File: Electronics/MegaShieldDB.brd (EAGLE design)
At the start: 100.3 x 80 mm, 40 parts, among them IC2 MCP4802, IC3 MCP4802, IC4 4013N, Q1 BF199, Q5 BF199, X1 M25-HD-20, X2 Brake, X4 Cruise Computers, X5 Steer, X6 Motor Controller

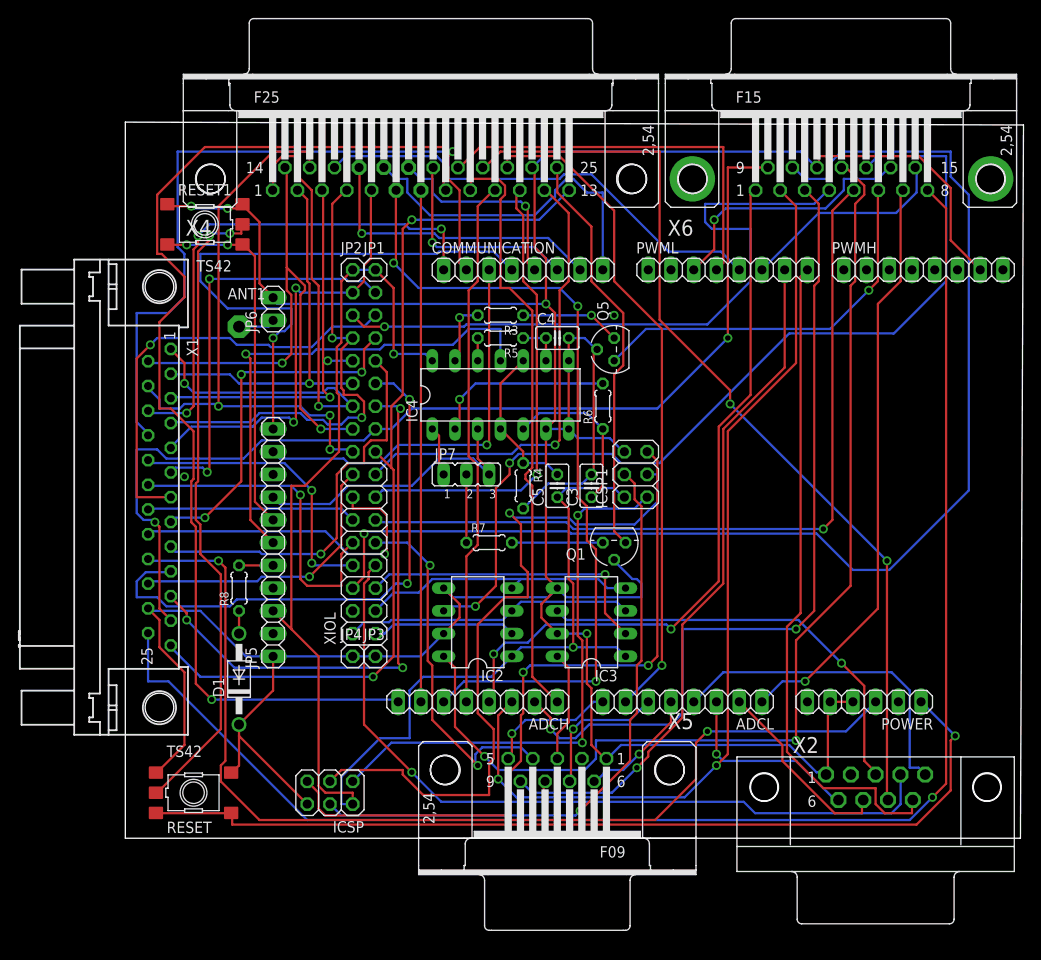
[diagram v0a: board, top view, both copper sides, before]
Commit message: Included holes for mounting Mega, board cutouts, renamed connectors. Signals to front panel have been swapped.  Connector names have changed.
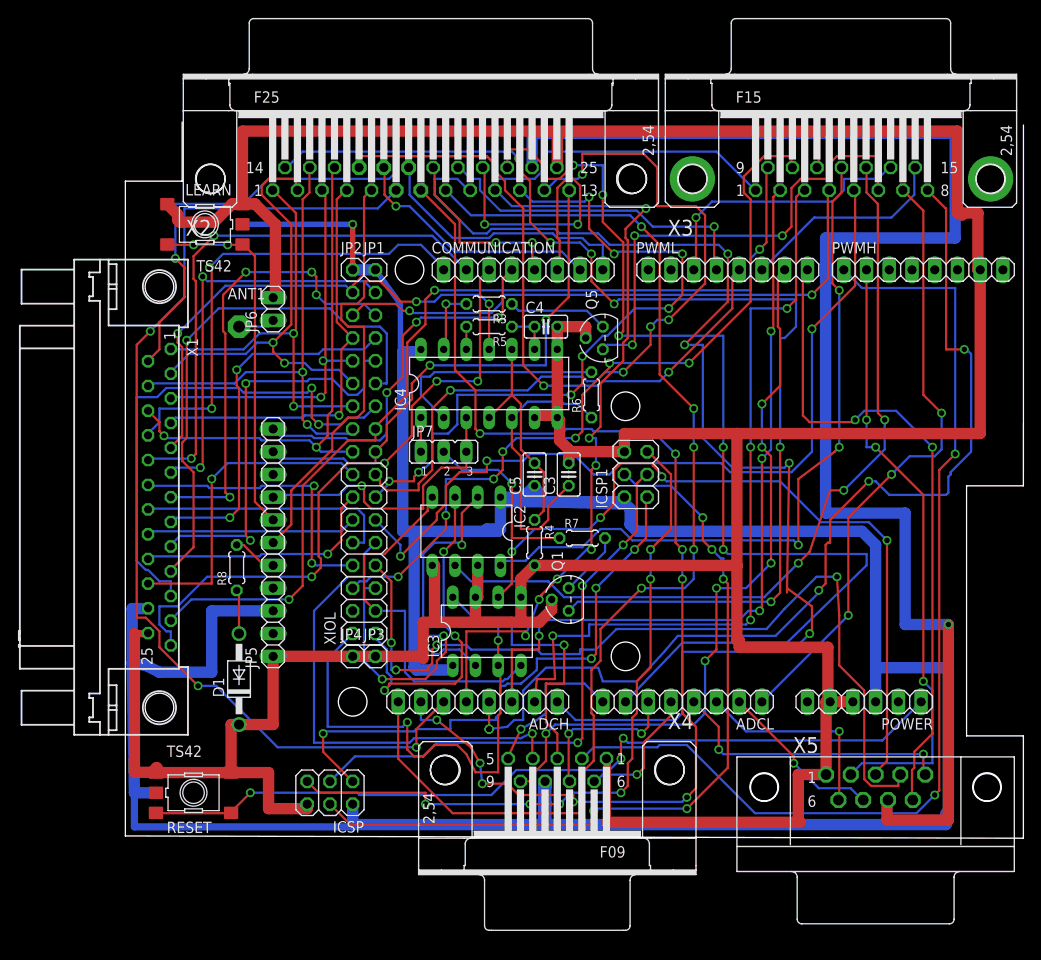
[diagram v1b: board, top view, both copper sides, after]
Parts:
- X2: value Brake -> Cruise Computers; device con-subd:182-009-MALE -> con-subd:F25H
- X4: value Cruise Computers -> Steer; device con-subd:F25H -> con-subd:F09H
- X5: value Steer -> Brake; device con-subd:F09H -> con-subd:182-009-MALE
- moved X2 92.6 mm to (33.0, 73.7)
- moved X4 67.8 mm to (48.3, 7.62), turned to 180 degrees
- moved X5 37.4 mm to (83.8, -3.81), turned to 0 degrees
- moved IC3 11.7 mm to (40.4, 23.1), turned to 0 degrees
- moved R7 10.4 mm to (51.1, 33.5)
- moved IC2 10.2 mm to (38.1, 34.3), turned to 180 degrees
- moved Q1 8.13 mm to (49.5, 26.7), turned to 90 degrees
- moved R4 6.48 mm to (45.7, 33.0)
- moved JP7 3.59 mm to (35.6, 43.2)
- moved C3 2.84 mm to (49.5, 40.6)
- moved C5 2.84 mm to (45.7, 40.6)
- moved R8 2.30 mm to (12.4, 30.2)
- moved R6 1.80 mm to (52.1, 49.5)
- moved Q5 1.80 mm to (53.3, 55.9)
- moved C4 1.80 mm to (47.0, 57.1)
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- renumbered RESET1 to LEARN, X6 to X3
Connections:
- removed net 5-GND: LEARN.5, RESET.5
- removed net VCC: POWER.3, X1.22, X5.8
- new net N$16: PWMH.2, X5.2
- new net N$17: PWMH.1, X4.2
- net +5V: now also LEARN.5, POWER.3, RESET.5, X1.24, X4.8
- net 5VBRK: now also X2.24, X5.8; no longer X2.8, X4.22
- net A1: now also X5.7; no longer X2.7
- net A11: now also X3.8; no longer X3.1
- net A12: now also X2.10; no longer X4.10
- net A13: now also X2.6; no longer X4.6
- net A14: now also X2.7; no longer X4.7
- net A15: now also X2.8; no longer X4.8
- net A4: now also X4.6; no longer X5.6
- net A5: now also X4.7; no longer X5.7
- net A6: now also X2.23; no longer X4.23
- net A7: now also X4.5; no longer X5.5
- net D14TXD3: now also X2.19; no longer X4.18
- net D15RXD3: now also X2.18; no longer X4.17
- net D16TXD2: now also X2.22; no longer X4.20
- net D17RXD2: now also X2.20; no longer X4.19
- net D20INT4: now also X1.18; no longer X1.17
- net D21INT5: now also X1.17; no longer X1.16
- net D23: now also X2.5; no longer X4.5
- net D27: now also X2.4; no longer X4.4
- net D29: now also X2.3; no longer X4.3
- net D31: now also X2.2; no longer X4.2
- net D33: now also X2.1; no longer X4.1
- net D35: now also X1.15, X2.15; no longer X1.14, X4.14
- net D36: now also X2.13; no longer X4.13
- net D37: now also X1.16, X2.16; no longer X1.15, X4.15
- net D39: now also X2.12; no longer X4.12
- net D3INT1: now also X2.21; no longer X4.21
- net D4: now also X2.17; no longer X4.16
- net D40: now also X1.22; no longer X1.21
- net D41: now also X2.11; no longer X4.11
- net D42: now also X1.21; no longer X1.20
- net D44: now also X1.20; no longer X1.19
- net D45: now also X4.4; no longer X5.4
- net D46: now also X1.19; no longer X1.18
- net D47: now also X5.4; no longer X2.4
- net D6: now also X4.9; no longer X5.9
- net D7: now also X5.9; no longer X2.9
- net DACC: now also X4.3; no longer X5.3
- net DACD: now also X5.3; no longer X2.3
- net FUEL: now also X1.14, X3.1; no longer X1.25, X3.8
- net GND: now also X1.25, X2.25, X4.1; no longer X1.24, X2.1, X4.24
- net N$1: now also X5.6; no longer X2.6
- net N$5: now also X2.9; no longer X4.9
- net N$8: now also X5.5; no longer X2.5
- net WLX: now also X2.14; no longer X4.25
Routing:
- net +5V: track 160.0 -> 352.0 mm, vias 2 -> 1
- net VCC: track 120.5 -> 0.00 mm, vias 2 -> 0
- net N$17: track 0.00 -> 114.9 mm, vias 0 -> 2
- net WLX: track 46.0 -> 128.6 mm, vias 0 -> 6
- net FUEL: track 169.8 -> 93.6 mm
- net A14: track 57.1 -> 130.2 mm, vias 0 -> 9
- net 5-GND: track 71.9 -> 0.00 mm, vias 2 -> 0
- net N$5: track 67.2 -> 136.2 mm, vias 0 -> 4
- net GND: track 390.8 -> 459.5 mm, vias 4 -> 0
- net N$16: track 0.00 -> 68.4 mm, vias 0 -> 3
- net 5VBRK: track 103.5 -> 165.2 mm, vias 2 -> 1
- net D48: track 138.8 -> 86.8 mm, vias 1 -> 7
- net A6: track 74.5 -> 122.1 mm, vias 1 -> 5
- net D52: track 32.4 -> 73.7 mm, vias 0 -> 3
- net DACA: track 119.6 -> 80.8 mm, vias 2 -> 3
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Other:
- outline, holes or cut-outs redrawn

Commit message: Mirrored Arduino pins for bottom mount. Added Wheel Revolution with pull-up resistor.
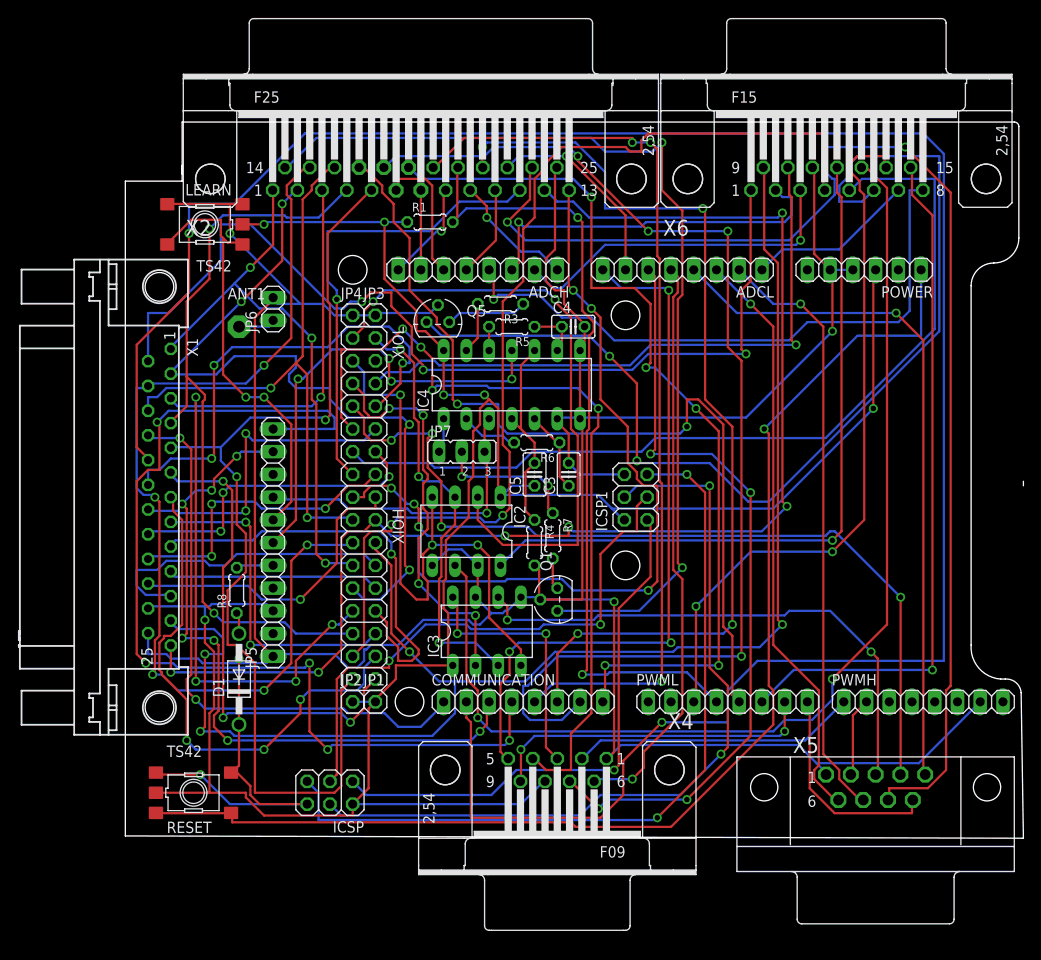
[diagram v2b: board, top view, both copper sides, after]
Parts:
- removed X3: Motor Controller, con-subd:F15HP
- added R1: 1M, rcl:0204/5
- added X6: (no value), con-subd:F15H
- moved ADCH 48.3 mm to (39.4, 63.5)
- moved ADCL 48.3 mm to (62.2, 63.5)
- moved COMMUNICATION 48.3 mm to (44.5, 15.2)
- moved JP1 48.3 mm to (27.9, 15.2)
- moved JP2 48.3 mm to (25.4, 15.2)
- moved POWER 48.3 mm to (82.5, 63.5)
- moved PWMH 48.3 mm to (89.2, 15.2)
- moved PWML 48.3 mm to (67.3, 15.2)
- moved JP3 38.1 mm to (27.9, 58.4)
- moved JP4 38.1 mm to (25.4, 58.4)
- moved XIOH 25.4 mm to (26.7, 26.7), flipped to the top, turned to 270 degrees
- moved Q5 18.5 mm to (34.9, 57.7), turned to 0 degrees
- moved XIOL 15.2 mm to (26.7, 47.0), turned to 270 degrees
- moved R6 8.10 mm to (46.0, 44.2), turned to 180 degrees
- moved R7 3.31 mm to (47.8, 33.8), turned to 270 degrees
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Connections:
- net N$16 renamed D9
- net N$17 renamed D8
- net +5V: now also R1.1
- net A0: now also X6.7; no longer X3.7
- net A10: now also X6.2; no longer X3.2
- net A11: now also X6.8; no longer X3.8
- net A9: now also X6.3; no longer X3.3
- net D25: now also X6.4; no longer X3.4
- net D2INT0: now also X6.14; no longer X3.14
- net D34: now also X6.9; no longer X3.9
- net D3INT1: now also R1.2
- net D43: now also X6.5; no longer X3.5
- net D48: now also X6.10; no longer X3.10
- net D5: now also X6.15; no longer X3.15
- net DACA: now also X6.12; no longer X3.12
- net DACB: now also X6.13; no longer X3.13
- net FUEL: now also X6.1; no longer X3.1
- net GND: now also X6.11; no longer X3.11
- net WLES: now also X6.6; no longer X3.6
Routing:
- net D20INT4: track 60.9 -> 254.3 mm
- net N$5: track 136.2 -> 14.2 mm, vias 4 -> 1
- net A14: track 130.2 -> 8.89 mm, vias 9 -> 0
- net A15: track 129.1 -> 11.5 mm, vias 5 -> 1
- net A13: track 117.0 -> 15.5 mm, vias 3 -> 0
- net D15RXD3: track 28.4 -> 128.0 mm, vias 1 -> 4
- net A6: track 122.1 -> 22.6 mm, vias 5 -> 1
- net +5V: track 352.0 -> 268.0 mm, vias 1 -> 6
- net D8: track 114.9 -> 31.9 mm, vias 2 -> 0
- net D17RXD2: track 21.0 -> 102.1 mm, vias 2 -> 3
- net A12: track 87.3 -> 10.4 mm, vias 7 -> 0
- net D16TXD2: track 34.0 -> 106.7 mm, vias 2 -> 4
- net D14TXD3: track 30.3 -> 100.7 mm, vias 0 -> 5
- net D18INT2: track 42.7 -> 112.4 mm, vias 3 -> 5
- net A5: track 17.9 -> 86.1 mm, vias 2 -> 4
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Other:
- outline, holes or cut-outs redrawn

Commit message: Rearranged jumper.
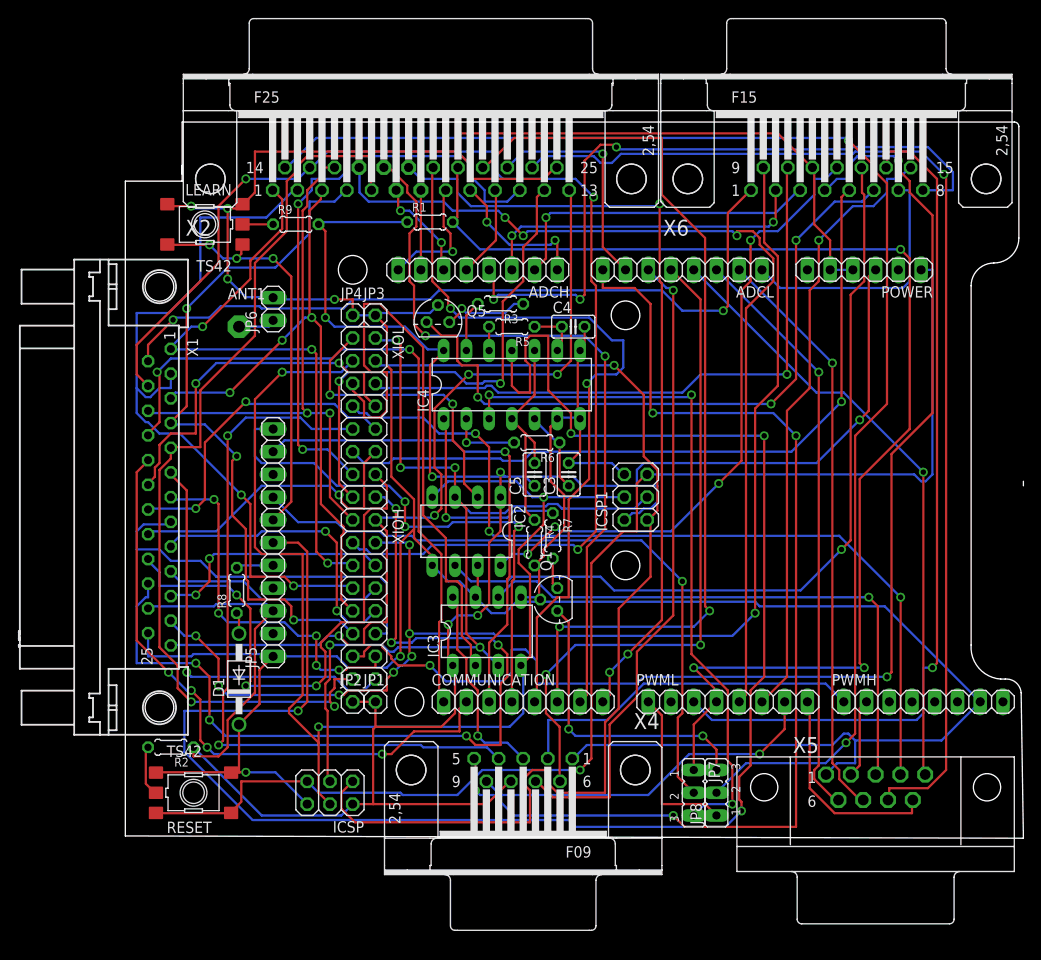
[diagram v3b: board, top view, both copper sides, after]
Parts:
- added JP8: (no value), jumper:JP2
- added R2, R9: 10M, rcl:0204/5
- JP7: value Latch -> (none)
- moved JP7 46.1 mm to (63.5, 5.08), turned to 270 degrees
- moved X4 3.81 mm to (44.5, 7.62)
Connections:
- net N$3 renamed RCVR5
- removed net N$11: JP7.2, R7.1
- removed net N$13: ICSP.5, ICSP1.5
- removed net N$14: ICSP.4, ICSP1.4
- removed net WLX: Q1.3, X2.14
- new net D0RX0: JP8.1, PWML.1
- new net N$6: R2.2, RESET.5
- new net WL2: JP5.8, JP7.2
- new net WLXCOLL: JP8.3, Q1.3
- new net X2-14: JP8.2, X2.14
- net +5V: now also R2.1, R9.2; no longer LEARN.5, RESET.5
- net CLKA: no longer JP5.8
- net D3INT1: now also JP7.1
- net D51: now also ICSP.4, ICSP1.4
- net D52: now also ICSP.3, ICSP1.3
- net N$10: now also LEARN.5, R9.1; no longer ICSP.3, ICSP1.3
- net N$2: now also R7.1; no longer JP7.1
- net N$9: now also XIOL.4
- net RESET: now also ICSP.5, ICSP1.5
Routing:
- net D20INT4: track 254.3 -> 69.3 mm, vias 2 -> 4
- net X2-14: track 0.00 -> 152.2 mm, vias 0 -> 2
- net CLKB: track 50.8 -> 198.1 mm
- net WLX: track 109.4 -> 0.00 mm, vias 2 -> 0
- net N$13: track 88.6 -> 0.00 mm, vias 2 -> 0
- net N$14: track 88.2 -> 0.00 mm, vias 2 -> 0
- net WL2: track 0.00 -> 74.2 mm, vias 0 -> 1
- net D51: track 65.9 -> 140.0 mm
- net D38: track 34.4 -> 99.2 mm, vias 1 -> 6
- net N$9: track 60.9 -> 121.1 mm
- net D39: track 116.4 -> 56.4 mm, vias 7 -> 2
- net N$10: track 61.9 -> 3.42 mm, vias 2 -> 0
- net D52: track 48.0 -> 103.3 mm, vias 3 -> 5
- net D18INT2: track 112.4 -> 59.7 mm, vias 5 -> 3
- net D3INT1: track 90.2 -> 139.9 mm, vias 2 -> 3
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
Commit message: update to Sourceforge 123
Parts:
- removed JP7, JP8: (no value), jumper:JP2
- removed LEARN, RESET: TS42, st-mod v1.4:TS42
- removed X6: (no value), con-subd:F15H
- added JP9: (no value), jumper:JP3Q
- added LSP1, LSP2: LSP13, solpad:LSP13
- added U$1, U$2: DPDT_DEV6X5MM_PAC, elcanoParts:NEWSWITCH2_PAC
- added X3: Motor, con-subd:182-015-MALE
- X1: value M25-HD-20 -> Panel
- X2: value Cruise Computers -> Cruise
- moved R9 68.8 mm to (79.7, 36.2), turned to 180 degrees
- moved JP6 51.3 mm to (26.7, 8.81), turned to 270 degrees
- moved ANT1 48.5 mm to (21.6, 9.51), turned to 180 degrees
- moved IC4 41.4 mm to (84.6, 51.7)
- moved R5 40.2 mm to (83.3, 59.4)
- moved C3 39.0 mm to (88.4, 37.8), turned to 0 degrees
- moved R6 38.9 mm to (84.8, 43.9)
- moved C4 35.8 mm to (85.1, 64.5), turned to 90 degrees
- moved IC2 34.3 mm to (71.6, 26.9), turned to 270 degrees
- moved R1 32.2 mm to (55.6, 44.8)
- moved IC3 31.7 mm to (66.8, 40.7), turned to 180 degrees
- moved D1 29.9 mm to (21.6, 46.3), turned to 270 degrees
- moved R3 27.7 mm to (69.3, 55.6), turned to 0 degrees
- moved Q1 26.8 mm to (34.8, 49.8), turned to 270 degrees
- moved R2 24.3 mm to (21.6, 27.9), turned to 270 degrees
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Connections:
- net A0: now also X3.7; no longer X6.7
- net A10: now also X3.2; no longer X6.2
- net A11: now also X3.8; no longer X6.8
- net A9: now also X3.3; no longer X6.3
- net CLKA: now also JP9.6; no longer JP7.3
- net D0RX0: now also JP9.1; no longer JP8.1
- net D25: now also X3.4; no longer X6.4
- net D2INT0: now also X3.14; no longer X6.14
- net D34: now also X3.9; no longer X6.9
- net D3INT1: now also JP9.2; no longer JP7.1
- net D43: now also X3.5; no longer X6.5
- net D48: now also X3.10; no longer X6.10
- net D5: now also X3.15; no longer X6.15
- net DACA: now also X3.12; no longer X6.12
- net DACB: now also X3.13; no longer X6.13
- net FUEL: now also X3.1; no longer X6.1
- net GND: now also U$1.PIN3, U$1.PIN6, U$2.PIN3, U$2.PIN6, X3.11; no longer LEARN.3, LEARN.4, RESET.1, RESET.2, X6.11
- net N$10: now also U$2.PIN1, U$2.PIN4; no longer LEARN.5
- net N$28: now also U$2.PIN2, U$2.PIN5; no longer LEARN.1, LEARN.2
- net N$6: now also U$1.PIN1, U$1.PIN4; no longer RESET.5
- net RESET: now also U$1.PIN2, U$1.PIN5; no longer RESET.3, RESET.4
- net WL2: now also JP9.4; no longer JP7.2
- net WLES: now also X3.6; no longer X6.6
- net WLXCOLL: now also JP9.5; no longer JP8.3
- net X2-14: now also JP9.3; no longer JP8.2
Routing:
- net X2-14: track 152.2 -> 24.3 mm, vias 2 -> 1
- net CLKB: track 198.1 -> 86.0 mm, vias 4 -> 2
- net FUEL: track 84.5 -> 193.7 mm, vias 2 -> 3
- net D27: track 78.9 -> 163.5 mm, vias 3 -> 5
- net D23: track 103.9 -> 187.6 mm, vias 2 -> 3
- net D35: track 139.0 -> 57.7 mm, vias 3 -> 2
- net D31: track 82.2 -> 161.1 mm, vias 2 -> 5
- net N$9: track 121.1 -> 55.7 mm, vias 1 -> 2
- net A10: track 37.3 -> 98.9 mm, vias 2 -> 1
- net A7: track 122.3 -> 63.3 mm, vias 4 -> 3
- net D36: track 95.2 -> 152.0 mm, vias 4 -> 8
- net D18INT2: track 59.7 -> 7.55 mm, vias 3 -> 0
- net D20INT4: track 69.3 -> 120.4 mm, vias 4 -> 5
- net D0RX0: track 18.7 -> 65.9 mm, vias 0 -> 4
- net D47: track 95.4 -> 142.6 mm, vias 3 -> 2
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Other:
- outline, holes or cut-outs redrawn

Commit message: noon changes of board design
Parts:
- moved X4 3.81 mm to (52.1, 7.62)
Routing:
- net GND: track 405.4 -> 0.00 mm, vias 6 -> 0
- net +5V: track 279.3 -> 0.00 mm, vias 5 -> 0
- net FUEL: track 193.7 -> 0.00 mm, vias 3 -> 0
- net D23: track 187.6 -> 0.00 mm, vias 3 -> 0
- net D27: track 163.5 -> 0.00 mm, vias 5 -> 0
- net D31: track 161.1 -> 0.00 mm, vias 5 -> 0
- net D36: track 152.0 -> 0.00 mm, vias 8 -> 0
- net D47: track 142.6 -> 0.00 mm, vias 2 -> 0
- net D34: track 130.8 -> 0.00 mm, vias 5 -> 0
- net 5VBRK: track 127.9 -> 0.00 mm
- net D51: track 125.2 -> 0.00 mm, vias 3 -> 0
- net RESET: track 120.9 -> 0.00 mm, vias 3 -> 0
- net D20INT4: track 120.4 -> 0.00 mm, vias 5 -> 0
- net D25: track 117.1 -> 0.00 mm, vias 1 -> 0
- net D52: track 111.4 -> 0.00 mm, vias 3 -> 0
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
